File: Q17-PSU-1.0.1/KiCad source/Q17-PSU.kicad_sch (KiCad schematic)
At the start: 30 parts, among them J1-1 AC1-1, J1-2 AC1-2, J1-3 AC2-1, J1-4 AC2-2, J2-1 V+, J2-1'1 V+, J2-2 GNDPWR, J2-2'1 GNDPWR, J2-3 V-, J2-4'1 V-

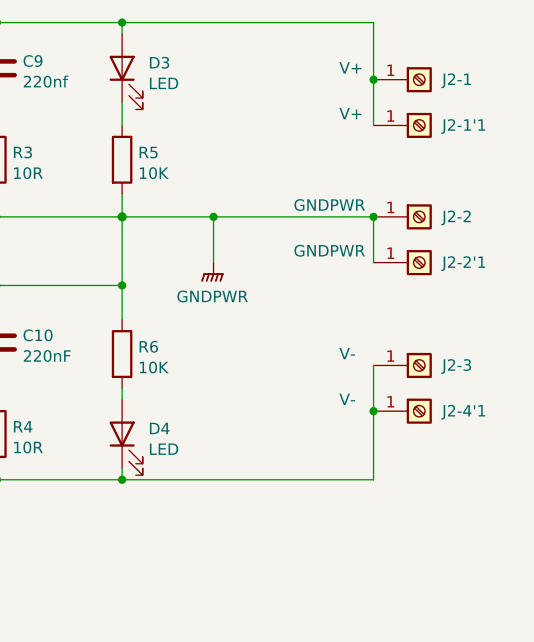
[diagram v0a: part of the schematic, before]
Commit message: Q17-PSU 1.0.1
Added one Faston connector on GND.
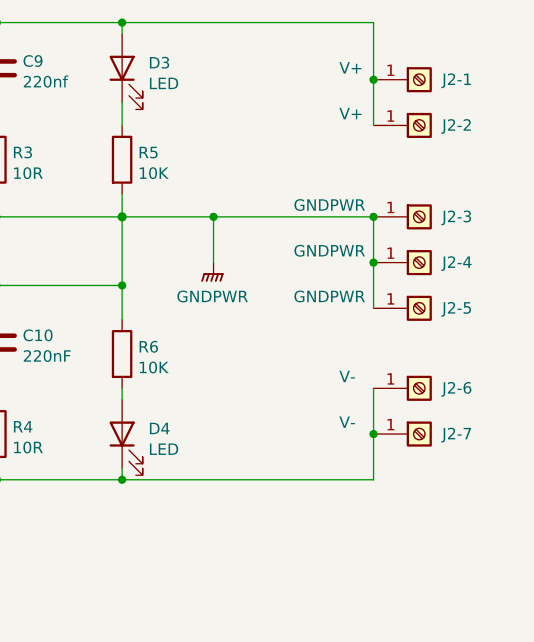
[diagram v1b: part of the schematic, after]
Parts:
- added J2-5: GNDPWR, Q17_Library:Faston_Connector_63849-1_TEC, symbol Connector:Screw_Terminal_01x01
- renumbered J2-1'1 to J2-2, J2-2 to J2-3, J2-2'1 to J2-4, J2-3 to J2-6, J2-4'1 to J2-7
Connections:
- net GNDPWR: now also J2-5.1 (Pin_1)
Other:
- moved on the sheet: J2-6, J2-7
